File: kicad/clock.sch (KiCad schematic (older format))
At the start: 10 parts, among them SW1 SW_Push, SW2 SW_SP3T, U5 74HC14, X1 1MHz Oscillator

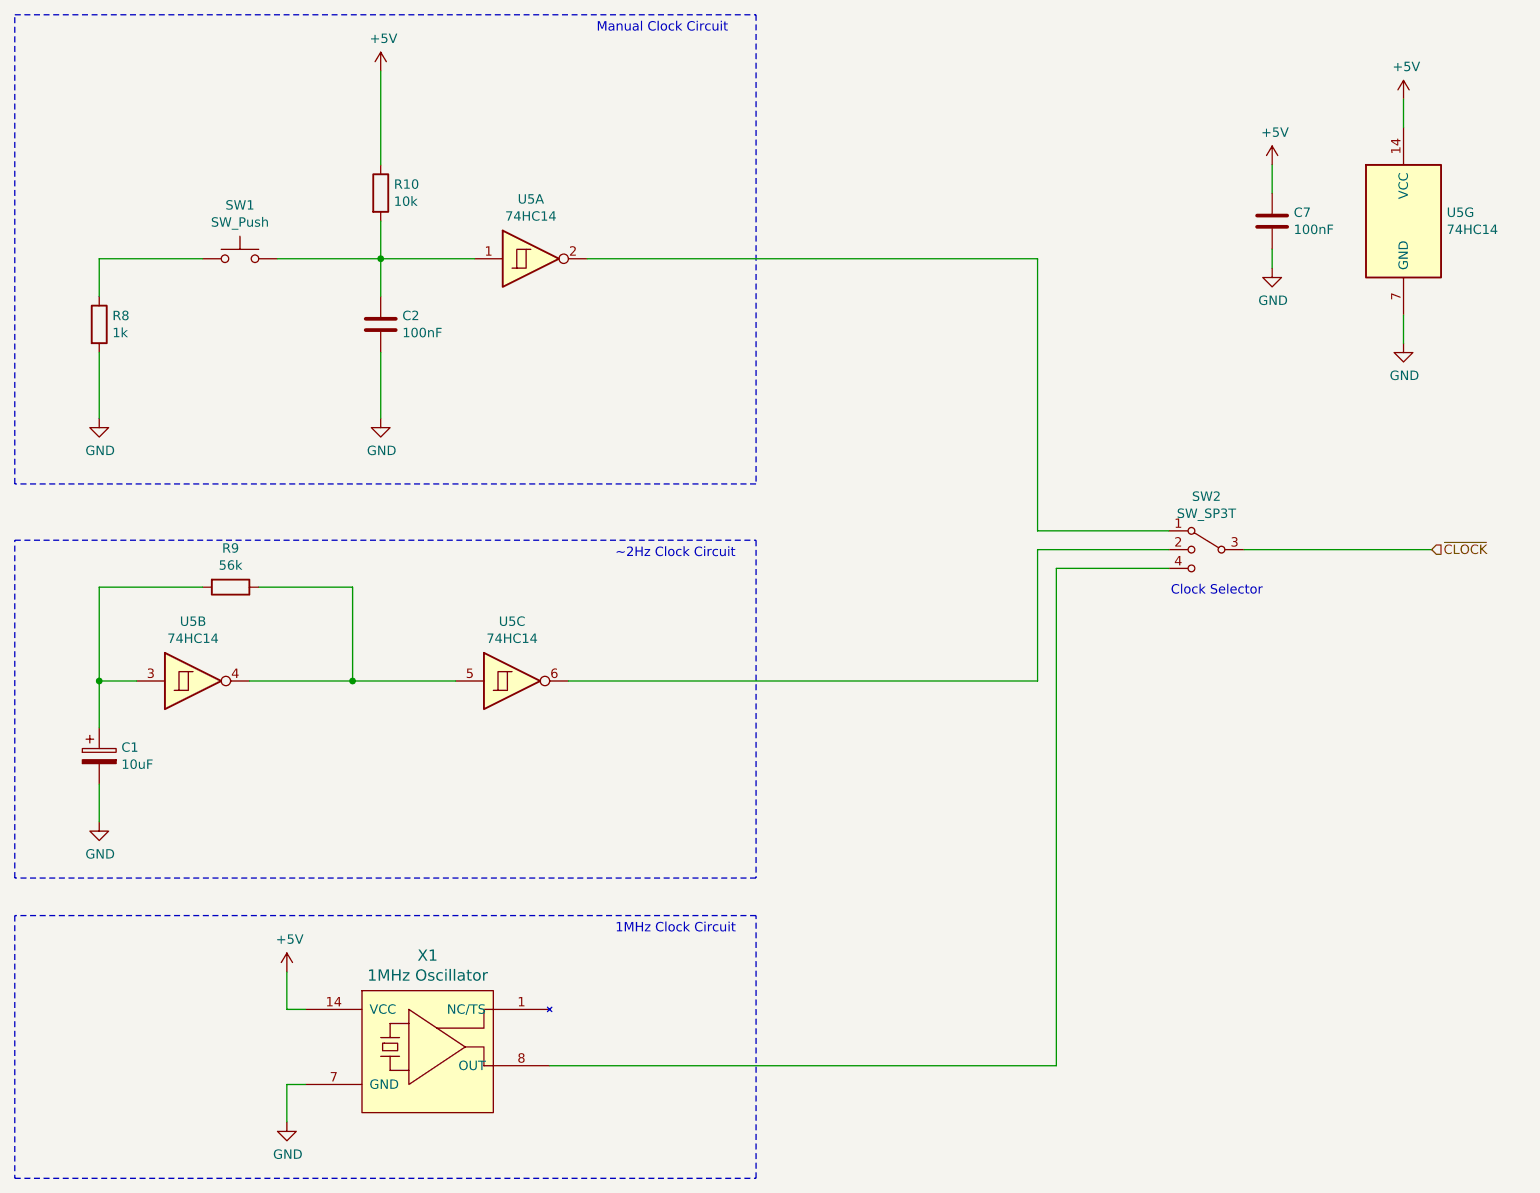
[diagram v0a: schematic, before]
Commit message: Added in extra LEDs to monitor signals with optional jumpers
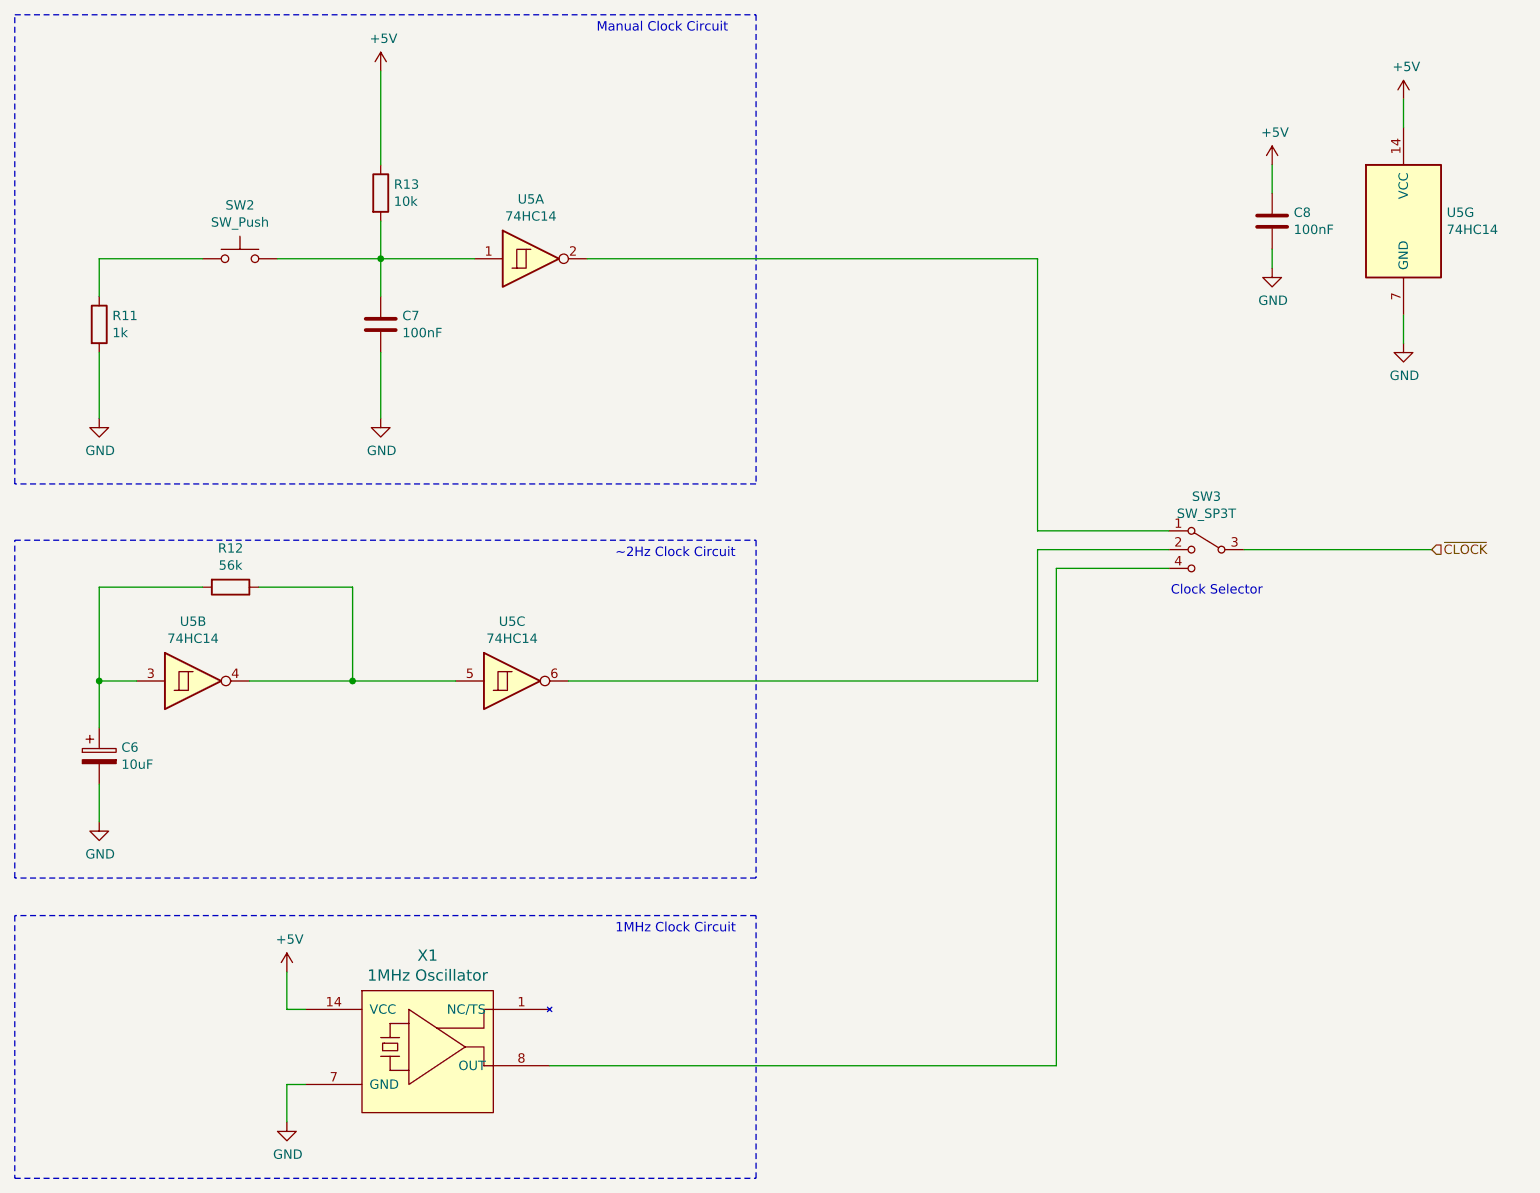
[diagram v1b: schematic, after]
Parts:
- renumbered C1 to C6, C2 to C7, C7 to C8, R8 to R11, R9 to R12, R10 to R13, SW1 to SW2, SW2 to SW3
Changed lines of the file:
@@
 $EndDescr
 $Comp
-L Whizz80:SW_SP3T SW2
+L Whizz80:SW_SP3T SW3
 U 1 1 5DE0A50E
 P 7900 3550
-F 0 "SW2" H 7900 3833 50  0000 C CNN
+F 0 "SW3" H 7900 3833 50  0000 C CNN
 F 1 "SW_SP3T" H 7900 3742 50  0000 C CNN
 F 2 "" H 7275 3725 50  0001 C CNN
@@
 $EndComp
 $Comp
-L Whizz80:R R10
+L Whizz80:R R13
 U 1 1 5DE46B7D
 P 3500 1650
-F 0 "R10" H 3570 1696 50  0000 L CNN
+F 0 "R13" H 3570 1696 50  0000 L CNN
 F 1 "10k" H 3570 1605 50  0000 L CNN
 F 2 "" V 3430 1650 50  0001 C CNN
@@
 $EndComp
 $Comp
-L Whizz80:R R8
+L Whizz80:R R11
 U 1 1 5DE47761
 P 2000 2350
-F 0 "R8" H 2070 2396 50  0000 L CNN
+F 0 "R11" H 2070 2396 50  0000 L CNN
 F 1 "1k" H 2070 2305 50  0000 L CNN
 F 2 "" V 1930 2350 50  0001 C CNN
@@
 $EndComp
 $Comp
-L Whizz80:R R9
+L Whizz80:R R12
 U 1 1 5DE47C08
 P 2700 3750
-F 0 "R9" V 2493 3750 50  0000 C CNN
+F 0 "R12" V 2493 3750 50  0000 C CNN
 F 1 "56k" V 2584 3750 50  0000 C CNN
 F 2 "" V 2630 3750 50  0001 C CNN
@@
 $EndComp
 $Comp
-L power:GND #PWR016
+L power:GND #PWR025
 U 1 1 5DE4B87C
 P 3000 6600
-F 0 "#PWR016" H 3000 6350 50  0001 C CNN
+F 0 "#PWR025" H 3000 6350 50  0001 C CNN
 F 1 "GND" H 3005 6427 50  0000 C CNN
 F 2 "" H 3000 6600 50  0001 C CNN
@@
 $EndComp
 $Comp
-L power:GND #PWR013
+L power:GND #PWR022
 U 1 1 5DE59101
 P 2000 2850
-F 0 "#PWR013" H 2000 2600 50  0001 C CNN
+F 0 "#PWR022" H 2000 2600 50  0001 C CNN
 F 1 "GND" H 2005 2677 50  0000 C CNN
 F 2 "" H 2000 2850 50  0001 C CNN
@@
 $EndComp
 $Comp
-L power:GND #PWR014
+L power:GND #PWR023
 U 1 1 5DE59BFC
 P 2000 5000
-F 0 "#PWR014" H 2000 4750 50  0001 C CNN
+F 0 "#PWR023" H 2000 4750 50  0001 C CNN
 F 1 "GND" H 2005 4827 50  0000 C CNN
 F 2 "" H 2000 5000 50  0001 C CNN
@@
 $EndComp
 $Comp
-L power:+5V #PWR015
+L power:+5V #PWR024
 U 1 1 5DE5AB3D
 P 3000 5800
-F 0 "#PWR015" H 3000 5650 50  0001 C CNN
+F 0 "#PWR024" H 3000 5650 50  0001 C CNN
 F 1 "+5V" H 3015 5973 50  0000 C CNN
 F 2 "" H 3000 5800 50  0001 C CNN
@@
 $EndComp
 $Comp
-L power:+5V #PWR017
+L power:+5V #PWR026
 U 1 1 5DE5D6BA
 P 3500 1000
-F 0 "#PWR017" H 3500 850 50  0001 C CNN
+F 0 "#PWR026" H 3500 850 50  0001 C CNN
 F 1 "+5V" H 3515 1173 50  0000 C CNN
 F 2 "" H 3500 1000 50  0001 C CNN
@@
 $EndComp
 $Comp
-L Whizz80:C C2
+L Whizz80:C C7
 U 1 1 5DE6382A
 P 3500 2350
-F 0 "C2" H 3615 2396 50  0000 L CNN
+F 0 "C7" H 3615 2396 50  0000 L CNN
 F 1 "100nF" H 3615 2305 50  0000 L CNN
 F 2 "" H 3538 2200 50  0001 C CNN
@@
 $EndComp
 $Comp
-L Whizz80:CP C1
+L Whizz80:CP C6
 U 1 1 5DE6464B
 P 2000 4650
-F 0 "C1" H 2118 4696 50  0000 L CNN
+F 0 "C6" H 2118 4696 50  0000 L CNN
 F 1 "10uF" H 2118 4605 50  0000 L CNN
 F 2 "" H 2038 4500 50  0001 C CNN
@@
 $EndComp
 $Comp
-L Whizz80:SW_Push SW1
+L Whizz80:SW_Push SW2
 U 1 1 5DE66258
 P 2750 2000
-F 0 "SW1" H 2750 2285 50  0000 C CNN
+F 0 "SW2" H 2750 2285 50  0000 C CNN
 F 1 "SW_Push" H 2750 2194 50  0000 C CNN
 F 2 "" H 2750 2200 50  0001 C CNN
@@
 $EndComp
 $Comp
-L power:GND #PWR018
+L power:GND #PWR027
 U 1 1 5DE66D9D
 P 3500 2850
-F 0 "#PWR018" H 3500 2600 50  0001 C CNN
+F 0 "#PWR027" H 3500 2600 50  0001 C CNN
 F 1 "GND" H 3505 2677 50  0000 C CNN
 F 2 "" H 3500 2850 50  0001 C CNN
@@
 $EndComp
 $Comp
-L Whizz80:C C7
+L Whizz80:C C8
 U 1 1 5E3603CA
 P 8250 1800
-F 0 "C7" H 8365 1846 50  0000 L CNN
+F 0 "C8" H 8365 1846 50  0000 L CNN
 F 1 "100nF" H 8365 1755 50  0000 L CNN
 F 2 "" H 8288 1650 50  0001 C CNN
@@
 $EndComp
 $Comp
-L power:+5V #PWR027
+L power:+5V #PWR028
 U 1 1 5E3613FC
 P 8250 1500
-F 0 "#PWR027" H 8250 1350 50  0001 C CNN
+F 0 "#PWR028" H 8250 1350 50  0001 C CNN
 F 1 "+5V" H 8265 1673 50  0000 C CNN
 F 2 "" H 8250 1500 50  0001 C CNN
@@
 $EndComp
 $Comp
-L power:+5V #PWR029
+L power:+5V #PWR030
 U 1 1 5E361E6D
 P 8950 1150
-F 0 "#PWR029" H 8950 1000 50  0001 C CNN
+F 0 "#PWR030" H 8950 1000 50  0001 C CNN
 F 1 "+5V" H 8965 1323 50  0000 C CNN
 F 2 "" H 8950 1150 50  0001 C CNN
@@
 $EndComp
 $Comp
-L power:GND #PWR028
+L power:GND #PWR029
 U 1 1 5E362668
 P 8250 2050
-F 0 "#PWR028" H 8250 1800 50  0001 C CNN
+F 0 "#PWR029" H 8250 1800 50  0001 C CNN
 F 1 "GND" H 8255 1877 50  0000 C CNN
 F 2 "" H 8250 2050 50  0001 C CNN
@@
 $EndComp
 $Comp
-L power:GND #PWR030
+L power:GND #PWR031
 U 1 1 5E362EEE
 P 8950 2450
-F 0 "#PWR030" H 8950 2200 50  0001 C CNN
+F 0 "#PWR031" H 8950 2200 50  0001 C CNN
 F 1 "GND" H 8955 2277 50  0000 C CNN
 F 2 "" H 8950 2450 50  0001 C CNN
